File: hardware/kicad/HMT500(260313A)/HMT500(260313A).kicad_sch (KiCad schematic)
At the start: 0 parts

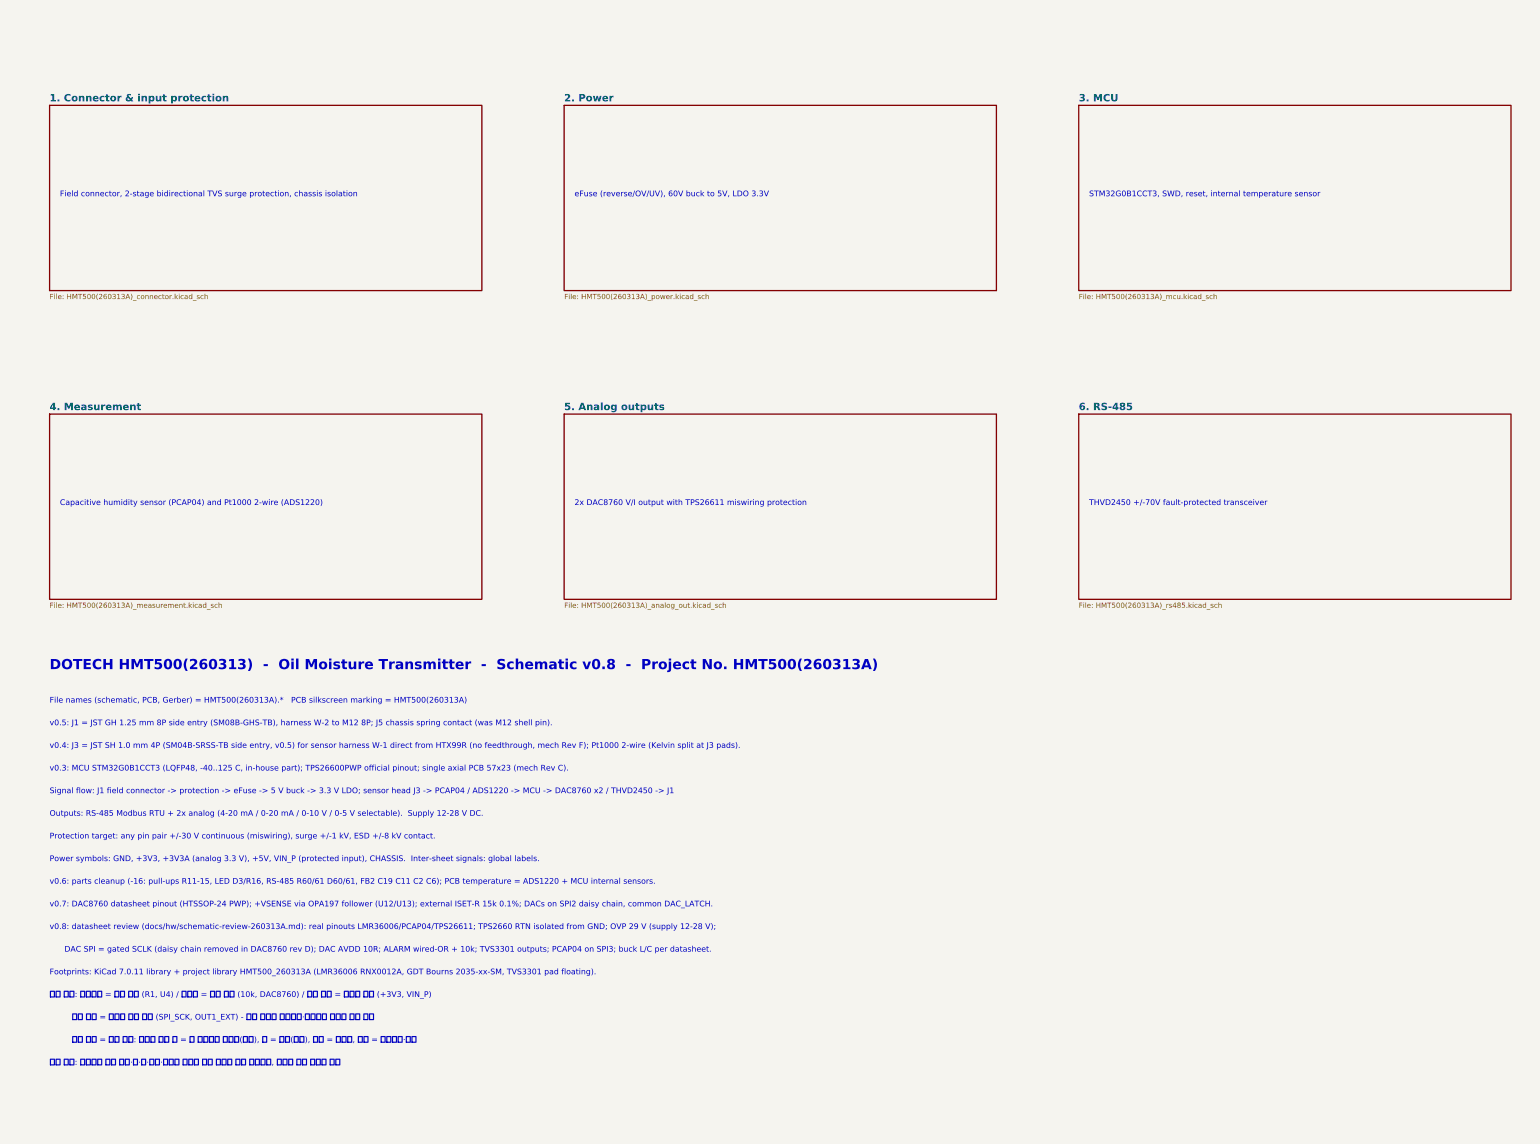
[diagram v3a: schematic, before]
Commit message: Schematic v0.9 + placement rev 4: apply triple-review A/B items, re-review fixes
- Power: OVP 32.6 V (R5 36.5k), D2 TVS3301, C2 2.2u 100V, buck input 220n x2,
  U2 pin 3 = SW; TPS26611 +Vs emitter-follower clamp (Q1 MMBTA06, R50, D50 27V)
- RS-485: THVD2410, DE 10k pull-down (R60) for in-house bootloader
- MCU: SGOOD on PA0/PA4, CS_CDC PA15, VIN_SENSE PB0, LATCH/CS pull-ups,
  SWD no-connect removed, netlist checker flags no-connect on used pins
- Analog: OPA197 V+ = DAC AVDD, R31/R41 100k, local caps; X7R throughout
- New aux sheet; SOT-23 and R1206 footprints; parts list and JLC files
- Placement: pin-targeted hints, MCU decaps under U4, chassis parts grouped
  in front, J5 keep-out 3.3 mm, CHASSIS netclass; 102/102 parts placed
- Docs: final review H table, decision #32, circuit design, placement rev 4

Co-Authored-By: Claude Opus 5.5 <noreply@anthropic.com>
Claude-Session: https://claude.ai/code/session_01JA2o8uJsqp9Vzsg4b665ev
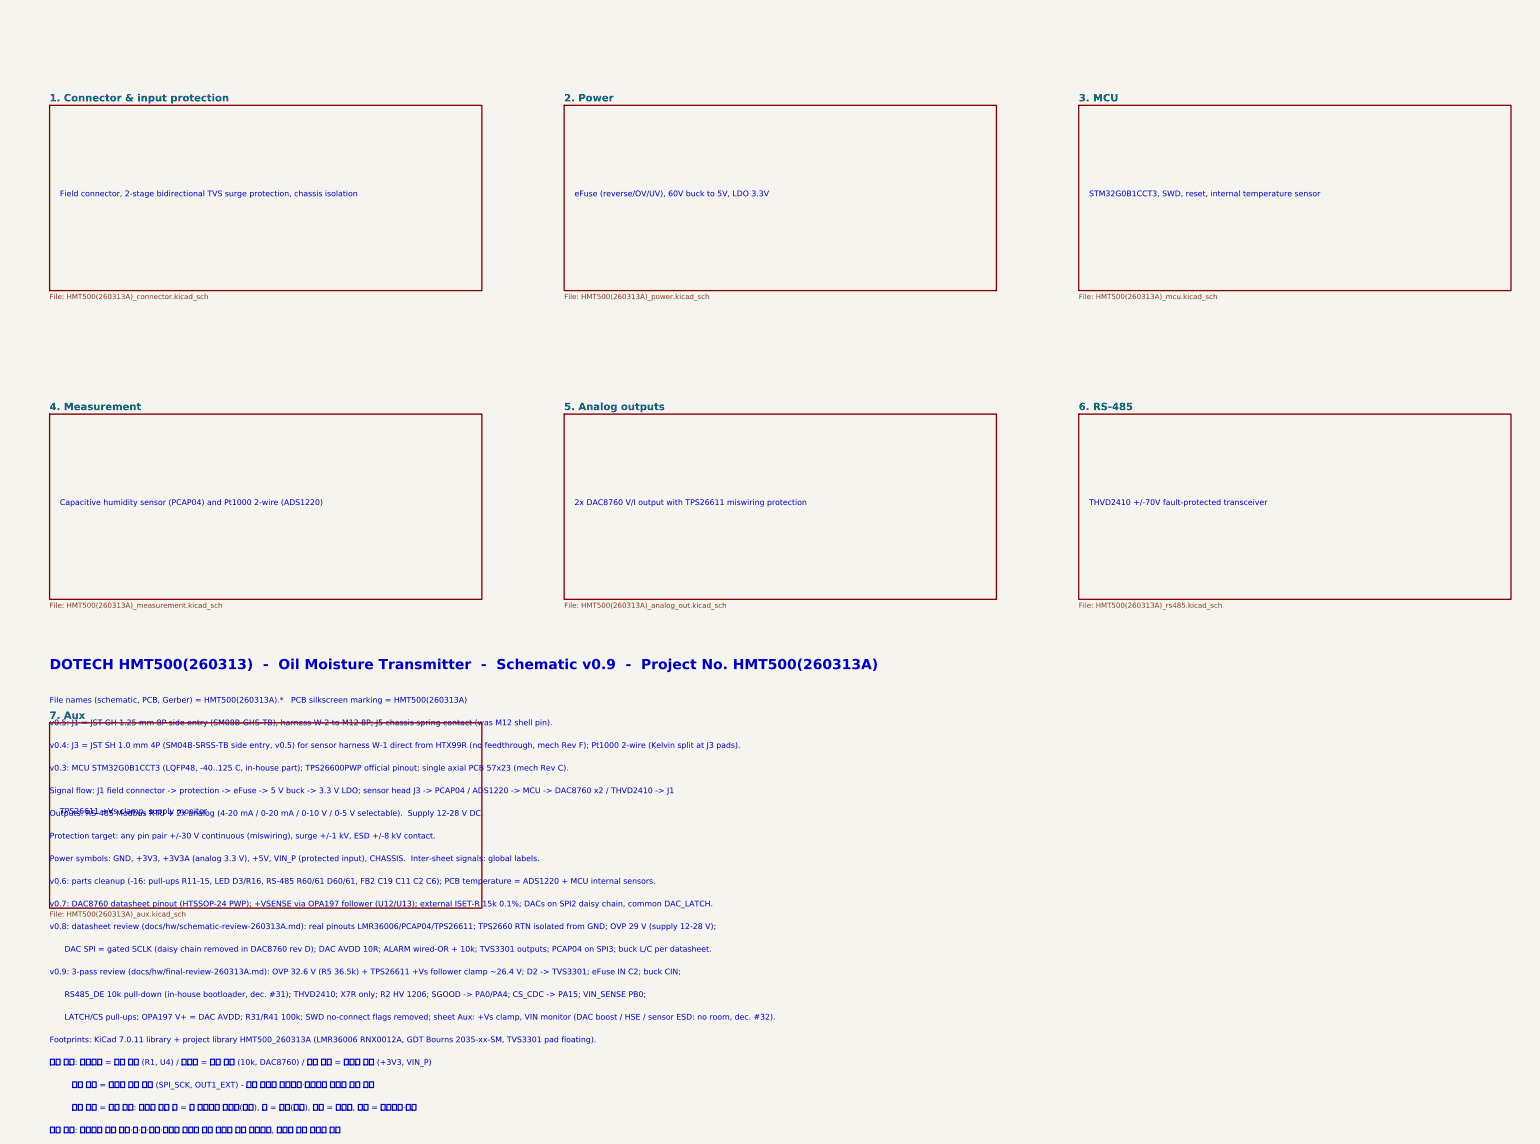
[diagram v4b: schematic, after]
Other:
- added sheet 7. Aux (HMT500(260313A)_aux.kicad_sch)
- note added: "DOTECH HMT500(260313) - Oil Moisture Transmitter - Schematic v0.9 - Project No. HMT500(260313A)"
- note added: "LATCH/CS pull-ups; OPA197 V+ = DAC AVDD; R31/R41 100k; SWD no-connect flags removed; sheet Aux: +Vs clamp, VIN monitor (DAC boost / HSE / sensor ESD: no room, dec. #32)."
- note added: "RS485_DE 10k pull-down (in-house bootloader, dec. #31); THVD2410; X7R only; R2 HV 1206; SGOOD -> PA0/PA4; CS_CDC -> PA15; VIN_SENSE PB0;"
- note added: "Signal flow: J1 field connector -> protection -> eFuse -> 5 V buck -> 3.3 V LDO; sensor head J3 -> PCAP04 / ADS1220 -> MCU -> DAC8760 x2 / THVD2410 -> J1"
- note added: "THVD2410 +/-70V fault-protected transceiver"
- note added: "TPS26611 +Vs clamp, supply monitor"
- note added: "v0.9: 3-pass review (docs/hw/final-review-260313A.md): OVP 32.6 V (R5 36.5k) + TPS26611 +Vs follower clamp ~26.4 V; D2 -> TVS3301; eFuse IN C2; buck CIN;"
- note removed: "DOTECH HMT500(260313) - Oil Moisture Transmitter - Schematic v0.8 - Project No. HMT500(260313A)"
- note removed: "Signal flow: J1 field connector -> protection -> eFuse -> 5 V buck -> 3.3 V LDO; sensor head J3 -> PCAP04 / ADS1220 -> MCU -> DAC8760 x2 / THVD2450 -> J1"
- note removed: "THVD2450 +/-70V fault-protected transceiver"
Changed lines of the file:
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@@
 (text "2x DAC8760 V/I output with TPS26611 miswiring protection" (at 160.02 154.94 0) (effects (font (size 1.4 1.4)) (justify left bottom)))
 (sheet (at 284.48 132.08) (size 106.68 45.72) (fields_autoplaced) (stroke (width 0.1524) (type solid)) (fill (color 0 0 0 0.0000)) (property "Sheetname" "6. RS-485" (at 284.48 131.318 0) (effects (font (size 1.8 1.8) bold) (justify left bottom))) (property "Sheetfile" "HMT500(260313A)_rs485.kicad_sch" (at 284.48 178.562 0) (effects (font (size 1.27 1.27)) (justify left top))) (instances (project "HMT500(260313A)" (path "/1ebb025b-11bd-5f7c-aaab-41e2a750e8b3" (page "7")))))
-(text "THVD2450 +/-70V fault-protected transceiver" (at 287.02 154.94 0) (effects (font (size 1.4 1.4)) (justify left bottom)))
-(text "DOTECH HMT500(260313)  -  Oil Moisture Transmitter  -  Schematic v0.8  -  Project No. HMT500(260313A)" (at 30.48 195.58 0) (effects (font (size 2.5 2.5) bold) (justify left bottom)))
+(text "THVD2410 +/-70V fault-protected transceiver" (at 287.02 154.94 0) (effects (font (size 1.4 1.4)) (justify left bottom)))
+(sheet (at 30.48 208.28) (size 106.68 45.72) (fields_autoplaced) (stroke (width 0.1524) (type solid)) (fill (color 0 0 0 0.0000)) (property "Sheetname" "7. Aux" (at 30.48 207.518 0) (effects (font (size 1.8 1.8) bold) (justify left bottom))) (property "Sheetfile" "HMT500(260313A)_aux.kicad_sch" (at 30.48 254.762 0) (effects (font (size 1.27 1.27)) (justify left top))) (instances (project "HMT500(260313A)" (path "/1ebb025b-11bd-5f7c-aaab-41e2a750e8b3" (page "8")))))
+(text "TPS26611 +Vs clamp, supply monitor" (at 33.02 231.14 0) (effects (font (size 1.4 1.4)) (justify left bottom)))
+(text "DOTECH HMT500(260313)  -  Oil Moisture Transmitter  -  Schematic v0.9  -  Project No. HMT500(260313A)" (at 30.48 195.58 0) (effects (font (size 2.5 2.5) bold) (justify left bottom)))
 (text "File names (schematic, PCB, Gerber) = HMT500(260313A).*   PCB silkscreen marking = HMT500(260313A)" (at 30.48 203.708 0) (effects (font (size 1.4 1.4)) (justify left bottom)))
 (text "v0.5: J1 = JST GH 1.25 mm 8P side entry (SM08B-GHS-TB), harness W-2 to M12 8P; J5 chassis spring contact (was M12 shell pin)." (at 30.48 209.296 0) (effects (font (size 1.4 1.4)) (justify left bottom)))
 (text "v0.4: J3 = JST SH 1.0 mm 4P (SM04B-SRSS-TB side entry, v0.5) for sensor harness W-1 direct from HTX99R (no feedthrough, mech Rev F); Pt1000 2-wire (Kelvin split at J3 pads)." (at 30.48 214.884 0) (effects (font (size 1.4 1.4)) (justify left bottom)))
 (text "v0.3: MCU STM32G0B1CCT3 (LQFP48, -40..125 C, in-house part); TPS26600PWP official pinout; single axial PCB 57x23 (mech Rev C)." (at 30.48 220.472 0) (effects (font (size 1.4 1.4)) (justify left bottom)))
-(text "Signal flow: J1 field connector -> protection -> eFuse -> 5 V buck -> 3.3 V LDO; sensor head J3 -> PCAP04 / ADS1220 -> MCU -> DAC8760 x2 / THVD2450 -> J1" (at 30.48 226.06 0) (effects (font (size 1.4 1.4)) (justify left bottom)))
+(text "Signal flow: J1 field connector -> protection -> eFuse -> 5 V buck -> 3.3 V LDO; sensor head J3 -> PCAP04 / ADS1220 -> MCU -> DAC8760 x2 / THVD2410 -> J1" (at 30.48 226.06 0) (effects (font (size 1.4 1.4)) (justify left bottom)))
 (text "Outputs: RS-485 Modbus RTU + 2x analog (4-20 mA / 0-20 mA / 0-10 V / 0-5 V selectable).  Supply 12-28 V DC." (at 30.48 231.648 0) (effects (font (size 1.4 1.4)) (justify left bottom)))
 (text "Protection target: any pin pair +/-30 V continuous (miswiring), surge +/-1 kV, ESD +/-8 kV contact." (at 30.48 237.236 0) (effects (font (size 1.4 1.4)) (justify left bottom)))
@@
 (text "v0.8: datasheet review (docs/hw/schematic-review-260313A.md): real pinouts LMR36006/PCAP04/TPS26611; TPS2660 RTN isolated from GND; OVP 29 V (supply 12-28 V);" (at 30.48 259.588 0) (effects (font (size 1.4 1.4)) (justify left bottom)))
 (text "      DAC SPI = gated SCLK (daisy chain removed in DAC8760 rev D); DAC AVDD 10R; ALARM wired-OR + 10k; TVS3301 outputs; PCAP04 on SPI3; buck L/C per datasheet." (at 30.48 265.176 0) (effects (font (size 1.4 1.4)) (justify left bottom)))
-(text "Footprints: KiCad 7.0.11 library + project library HMT500_260313A (LMR36006 RNX0012A, GDT Bourns 2035-xx-SM, TVS3301 pad floating)." (at 30.48 270.764 0) (effects (font (size 1.4 1.4)) (justify left bottom)))
-(text "표기 규칙: 부품번호 = 굵은 글자 (R1, U4) / 부품값 = 보통 글자 (10k, DAC8760) / 전원 네트 = 기울인 글자 (+3V3, VIN_P)" (at 30.48 276.352 0) (effects (font (face "NanumGothic") (size 1.4 1.4)) (justify left bottom)))
-(text "         신호 네트 = 테두리 있는 라벨 (SPI_SCK, OUT1_EXT) - 네트 이름은 부품번호·부품명과 겹치지 않게 지음" (at 30.48 281.94 0) (effects (font (face "NanumGothic") (size 1.4 1.4)) (justify left bottom)))
-(text "         라벨 모양 = 신호 방향: 뾰족한 쪽이 밖 = 이 시트에서 내보냄(출력), 안 = 받음(입력), 양쪽 = 양방향, 네모 = 아날로그·수동" (at 30.48 287.528 0) (effects (font (face "NanumGothic") (size 1.4 1.4)) (justify left bottom)))
-(text "글자 겹침: 생성기가 부품 몸체·핀·선·라벨·메모와 겹치지 않는 자리에 자동 배치하고, 겹치면 생성 실패로 처리" (at 30.48 293.116 0) (effects (font (face "NanumGothic") (size 1.4 1.4)) (justify left bottom)))
+(text "v0.9: 3-pass review (docs/hw/final-review-260313A.md): OVP 32.6 V (R5 36.5k) + TPS26611 +Vs follower clamp ~26.4 V; D2 -> TVS3301; eFuse IN C2; buck CIN;" (at 30.48 270.764 0) (effects (font (size 1.4 1.4)) (justify left bottom)))
+(text "      RS485_DE 10k pull-down (in-house bootloader, dec. #31); THVD2410; X7R only; R2 HV 1206; SGOOD -> PA0/PA4; CS_CDC -> PA15; VIN_SENSE PB0;" (at 30.48 276.352 0) (effects (font (size 1.4 1.4)) (justify left bottom)))
+(text "      LATCH/CS pull-ups; OPA197 V+ = DAC AVDD; R31/R41 100k; SWD no-connect flags removed; sheet Aux: +Vs clamp, VIN monitor (DAC boost / HSE / sensor ESD: no room, dec. #32)." (at 30.48 281.94 0) (effects (font (size 1.4 1.4)) (justify left bottom)))
+(text "Footprints: KiCad 7.0.11 library + project library HMT500_260313A (LMR36006 RNX0012A, GDT Bourns 2035-xx-SM, TVS3301 pad floating)." (at 30.48 287.528 0) (effects (font (size 1.4 1.4)) (justify left bottom)))
+(text "표기 규칙: 부품번호 = 굵은 글자 (R1, U4) / 부품값 = 보통 글자 (10k, DAC8760) / 전원 네트 = 기울인 글자 (+3V3, VIN_P)" (at 30.48 293.116 0) (effects (font (face "NanumGothic") (size 1.4 1.4)) (justify left bottom)))
+(text "         신호 네트 = 테두리 있는 라벨 (SPI_SCK, OUT1_EXT) - 네트 이름은 부품번호·부품명과 겹치지 않게 지음" (at 30.48 298.704 0) (effects (font (face "NanumGothic") (size 1.4 1.4)) (justify left bottom)))
+(text "         라벨 모양 = 신호 방향: 뾰족한 쪽이 밖 = 이 시트에서 내보냄(출력), 안 = 받음(입력), 양쪽 = 양방향, 네모 = 아날로그·수동" (at 30.48 304.292 0) (effects (font (face "NanumGothic") (size 1.4 1.4)) (justify left bottom)))
+(text "글자 겹침: 생성기가 부품 몸체·핀·선·라벨·메모와 겹치지 않는 자리에 자동 배치하고, 겹치면 생성 실패로 처리" (at 30.48 309.88 0) (effects (font (face "NanumGothic") (size 1.4 1.4)) (justify left bottom)))
 (sheet_instances (path "/" (page "1")))
 )

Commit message: Schematic v0.9 PDF: root sheet 4x2 layout, rev 0.9 in title blocks
Seven sheet boxes no longer overlap the notes, notes stay on the page
(v0.3-v0.8 history moved to one line pointing to the decision log).

Co-Authored-By: Claude Opus 5.5 <noreply@anthropic.com>
Claude-Session: https://claude.ai/code/session_01JA2o8uJsqp9Vzsg4b665ev
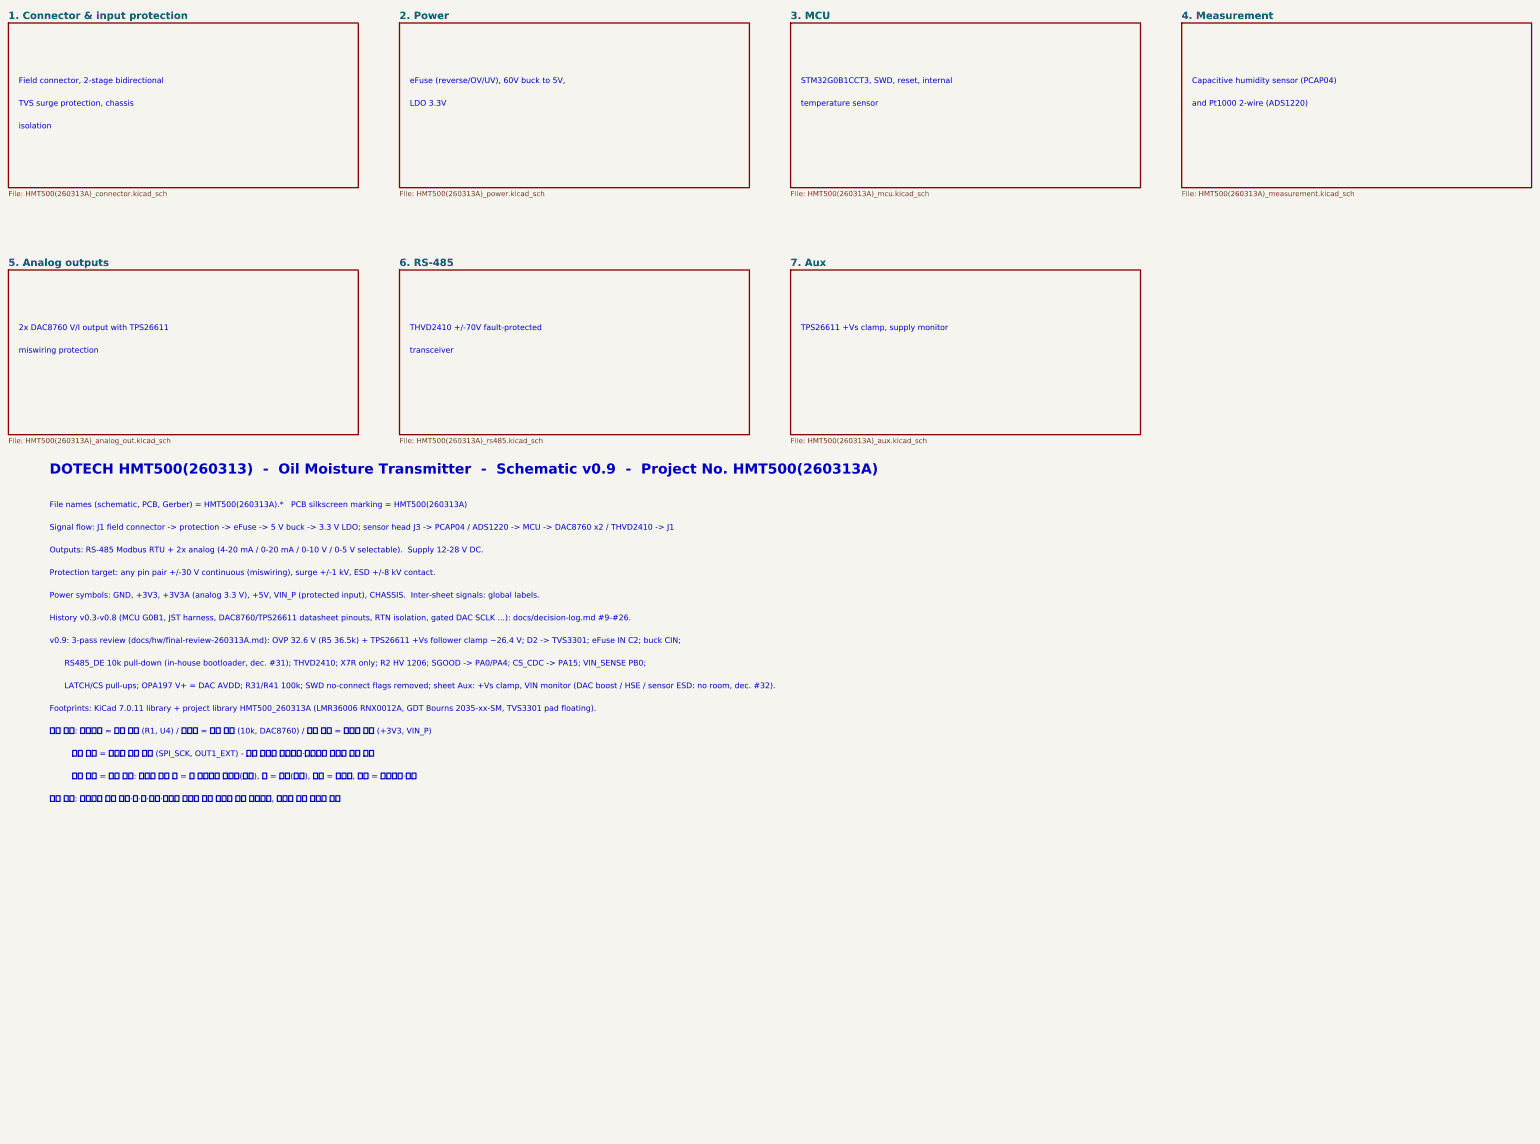
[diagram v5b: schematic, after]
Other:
- note added: "2x DAC8760 V/I output with TPS26611"
- note added: "Capacitive humidity sensor (PCAP04)"
- note added: "Field connector, 2-stage bidirectional"
- note added: "History v0.3-v0.8 (MCU G0B1, JST harness, DAC8760/TPS26611 datasheet pinouts, RTN isolation, gated DAC SCLK ...): docs/decision-log.md #9-#26."
- note added: "LDO 3.3V"
- note added: "STM32G0B1CCT3, SWD, reset, internal"
- note added: "THVD2410 +/-70V fault-protected"
- note added: "TVS surge protection, chassis"
- note added: "and Pt1000 2-wire (ADS1220)"
- note added: "eFuse (reverse/OV/UV), 60V buck to 5V,"
- note added: "isolation"
- note added: "miswiring protection"
- note added: "temperature sensor"
- note added: "transceiver"
- note removed: "2x DAC8760 V/I output with TPS26611 miswiring protection"
- note removed: "Capacitive humidity sensor (PCAP04) and Pt1000 2-wire (ADS1220)"
- note removed: "DAC SPI = gated SCLK (daisy chain removed in DAC8760 rev D); DAC AVDD 10R; ALARM wired-OR + 10k; TVS3301 outputs; PCAP04 on SPI3; buck L/C per datasheet."
- note removed: "Field connector, 2-stage bidirectional TVS surge protection, chassis isolation"
- note removed: "STM32G0B1CCT3, SWD, reset, internal temperature sensor"
- note removed: "THVD2410 +/-70V fault-protected transceiver"
- note removed: "eFuse (reverse/OV/UV), 60V buck to 5V, LDO 3.3V"
- note removed: "v0.3: MCU STM32G0B1CCT3 (LQFP48, -40..125 C, in-house part); TPS26600PWP official pinout; single axial PCB 57x23 (mech Rev C)."
- note removed: "v0.4: J3 = JST SH 1.0 mm 4P (SM04B-SRSS-TB side entry, v0.5) for sensor harness W-1 direct from HTX99R (no feedthrough, mech Rev F); Pt1000 2-wire (Kelvin split at J3 pads)."
- note removed: "v0.5: J1 = JST GH 1.25 mm 8P side entry (SM08B-GHS-TB), harness W-2 to M12 8P; J5 chassis spring contact (was M12 shell pin)."
- note removed: "v0.6: parts cleanup (-16: pull-ups R11-15, LED D3/R16, RS-485 R60/61 D60/61, FB2 C19 C11 C2 C6); PCB temperature = ADS1220 + MCU internal sensors."
- note removed: "v0.7: DAC8760 datasheet pinout (HTSSOP-24 PWP); +VSENSE via OPA197 follower (U12/U13); external ISET-R 15k 0.1%; DACs on SPI2 daisy chain, common DAC_LATCH."
- note removed: "v0.8: datasheet review (docs/hw/schematic-review-260313A.md): real pinouts LMR36006/PCAP04/TPS26611; TPS2660 RTN isolated from GND; OVP 29 V (supply 12-28 V);"
